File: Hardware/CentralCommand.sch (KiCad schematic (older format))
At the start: 17 parts, among them IC101 STM32F030C8, P101 I2C, P102 GPIO1, P103 GPIO1, P104 USART, P105 SPI, P106 ADC, Y101 8Mhz

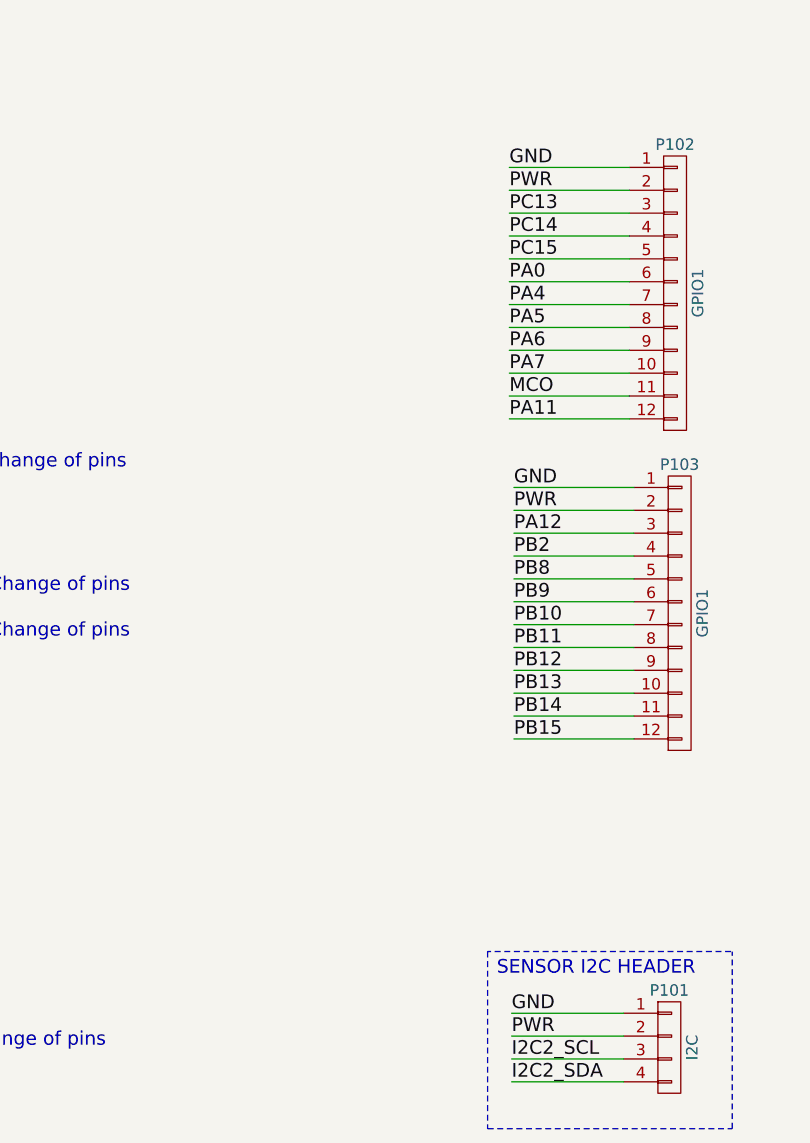
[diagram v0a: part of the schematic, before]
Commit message: swapped power and gnd on gpio headers and added blinky led
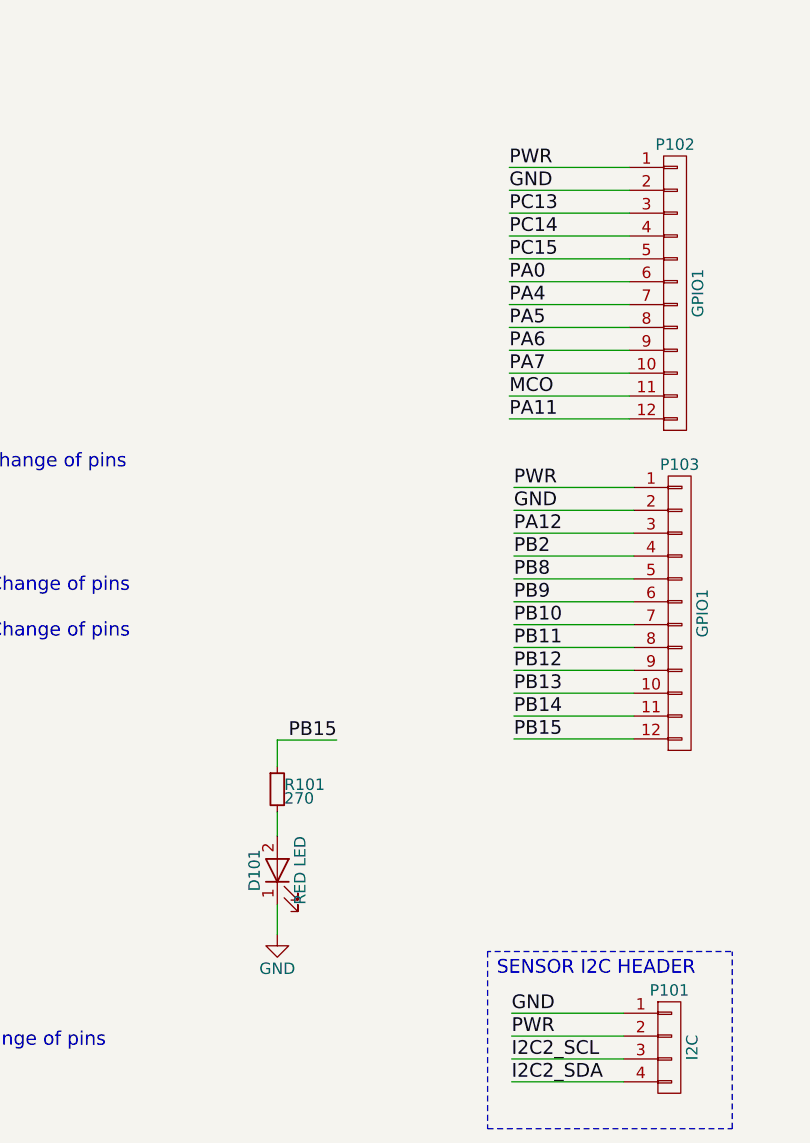
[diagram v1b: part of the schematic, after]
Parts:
- added D101: RED LED, LEDs:LED_0805, symbol LED
- added R101: 270, Resistors_SMD:R_0805, symbol R_Small
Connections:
- net GND: now also P102.2 (P2), P103.2 (P2), D101.1 (K); no longer P102.1 (P1), P103.1 (P1)
- net PB15: now also R101.1
- net PWR: now also P102.1 (P1), P103.1 (P1); no longer P102.2 (P2), P103.2 (P2)
- new net: D101.2 (A), R101.2
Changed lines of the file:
@@
 Text Label 2950 6485 0    60   ~ 0
 GND
-Text Label 7255 1265 0    60   ~ 0
+Text Label 7255 1365 0    60   ~ 0
 GND
 Text Label 10225 3100 2    60   ~ 0
@@
 Wire Wire Line
 	7780 1365 7255 1365
-Text Label 7255 1365 0    60   ~ 0
+Text Label 7255 1265 0    60   ~ 0
 PWR
 $Comp
@@
 Wire Wire Line
 	7800 2665 7275 2665
-Text Label 7275 2665 0    60   ~ 0
+Text Label 7275 2765 0    60   ~ 0
 GND
 Wire Wire Line
 	7800 2765 7275 2765
-Text Label 7275 2765 0    60   ~ 0
+Text Label 7275 2665 0    60   ~ 0
 PWR
+$Comp
+L R_Small R101
+U 1 1 5914C21D
+P 6240 3985
+F 0 "R101" H 6270 4005 50  0000 L CNN
+F 1 "270" H 6270 3945 50  0000 L CNN
+F 2 "Resistors_SMD:R_0805" H 6240 3985 50  0001 C CNN
+F 3 "" H 6240 3985 50  0000 C CNN
+F 4 "Value" H 6240 3985 60  0001 C CNN "Fieldname"
+	1    6240 3985
+	1    0    0    -1
+$EndComp
+$Comp
+L LED D101
+U 1 1 5914C488
+P 6240 4340
+F 0 "D101" H 6240 4440 50  0000 C CNN
+F 1 "RED LED" H 6240 4240 50  0000 C CNN
+F 2 "LEDs:LED_0805" H 6240 4340 50  0001 C CNN
+F 3 "" H 6240 4340 50  0000 C CNN
+F 4 "Value" H 6240 4340 60  0001 C CNN "Fieldname"
+	1    6240 4340
+	0    -1   -1   0
+$EndComp
+$Comp
+L GND #PWR09
+U 1 1 5914C558
+P 6240 4620
+F 0 "#PWR09" H 6240 4370 50  0001 C CNN
+F 1 "GND" H 6240 4470 50  0000 C CNN
+F 2 "" H 6240 4620 50  0000 C CNN
+F 3 "" H 6240 4620 50  0000 C CNN
+	1    6240 4620
+	1    0    0    -1
+$EndComp
+Wire Wire Line
+	6240 4085 6240 4190
+Wire Wire Line
+	6240 4490 6240 4620
+Wire Wire Line
+	6240 3885 6240 3770
+Wire Wire Line
+	6240 3770 6500 3770
+Text Label 6500 3770 2    60   ~ 0
+PB15
 $EndSCHEMATC

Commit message: more layout
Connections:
- net MCO: now also P103.10 (P10); no longer P102.11 (P11)
- net PA11: now also P103.11 (P11); no longer P102.12 (P12)
- net PA12: now also P103.12 (P12); no longer P103.3 (P3)
- net PB10: now also P102.12 (P12), R101.1; no longer P103.7 (P7)
- net PB11: now also P103.3 (P3); no longer P103.8 (P8)
- net PB12: now also P103.4 (P4); no longer P103.9 (P9)
- net PB13: now also P103.5 (P5); no longer P103.10 (P10)
- net PB14: now also P103.6 (P6); no longer P103.11 (P11)
- net PB15: now also P103.7 (P7); no longer P103.12 (P12), R101.1
- net PB2: now also P102.11 (P11); no longer P103.4 (P4)
- net PB8: now also P103.8 (P8); no longer P103.5 (P5)
- net PB9: now also P103.9 (P9); no longer P103.6 (P6)
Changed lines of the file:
@@
 Text Label 7255 2165 0    60   ~ 0
 PA7
+Text Label 7275 3665 0    60   ~ 0
+PA11
+Text Label 7275 3765 0    60   ~ 0
+PA12
+Text Label 7255 2265 0    60   ~ 0
+PB2
+Text Label 7275 3365 0    60   ~ 0
+PB8
+Text Label 7275 3465 0    60   ~ 0
+PB9
 Text Label 7255 2365 0    60   ~ 0
-PA11
+PB10
 Text Label 7275 2865 0    60   ~ 0
-PA12
+PB11
 Text Label 7275 2965 0    60   ~ 0
-PB2
+PB12
 Text Label 7275 3065 0    60   ~ 0
-PB8
+PB13
 Text Label 7275 3165 0    60   ~ 0
-PB9
+PB14
 Text Label 7275 3265 0    60   ~ 0
-PB10
-Text Label 7275 3365 0    60   ~ 0
-PB11
-Text Label 7275 3465 0    60   ~ 0
-PB12
+PB15
 Text Label 7275 3565 0    60   ~ 0
-PB13
-Text Label 7275 3665 0    60   ~ 0
-PB14
-Text Label 7275 3765 0    60   ~ 0
-PB15
-Text Label 7255 2265 0    60   ~ 0
 MCO
 Text Notes 2870 1600 0    60   ~ 0
@@
 	6240 3770 6500 3770
 Text Label 6500 3770 2    60   ~ 0
-PB15
+PB10
 $EndSCHEMATC
